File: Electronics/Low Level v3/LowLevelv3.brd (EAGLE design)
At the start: 116.8 x 69.8 mm, 65 parts, among them IC2 MCP4802, K1 ORWH-SH-105D1F,000, K3 ORWH-SH-105D1F,000, Q1 16MHz, T1 2N3904, T2 2N3904, U1 284512-4, U4 MCP2515, U5 MCP2551DIL08, X3 Motor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

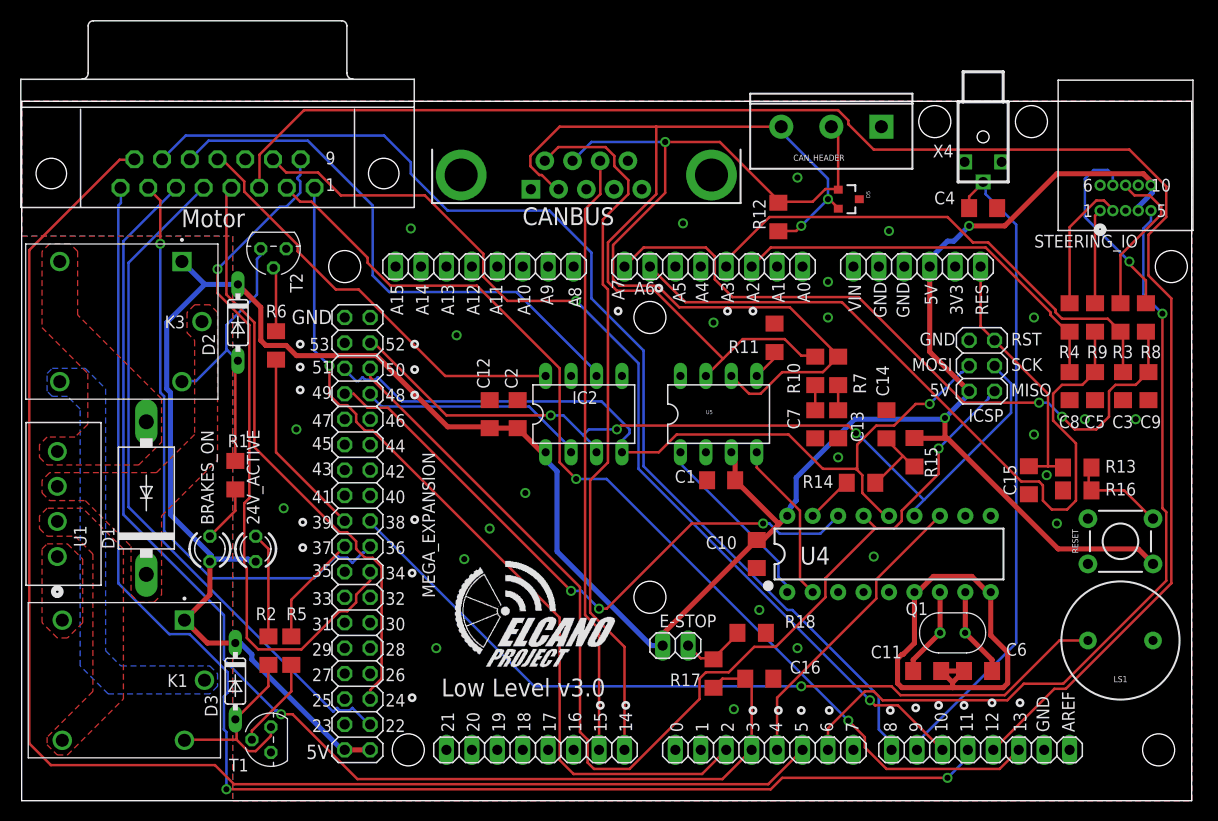
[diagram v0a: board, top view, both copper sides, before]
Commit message: re-routed watchdog from digi-5 to DB15 thru middle instead of along edge
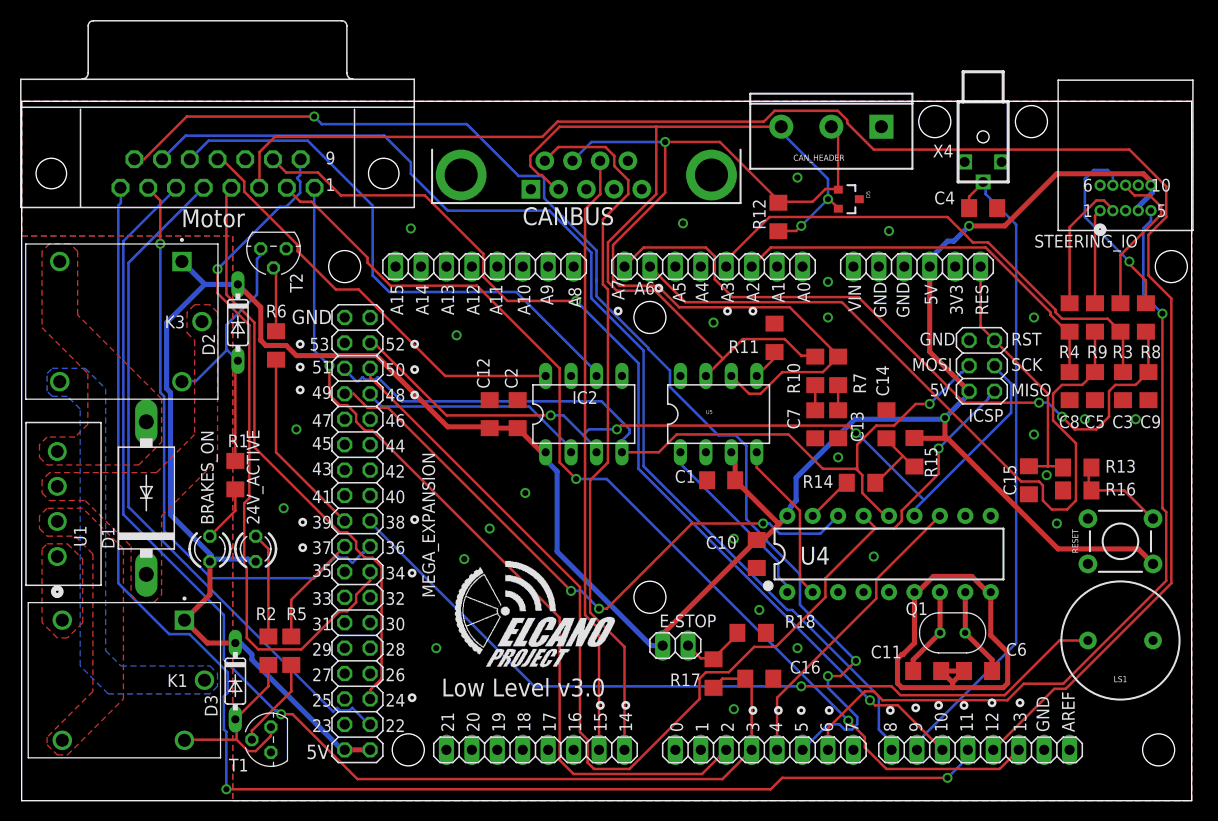
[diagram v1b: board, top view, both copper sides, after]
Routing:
- net WATCHDOG: track 143.8 -> 123.7 mm, vias 0 -> 3
- net GND: vias 25 -> 26
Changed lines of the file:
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@@
 <circle x="73.025" y="9.017" radius="0.315628125" width="0.254" layer="25"/>
 <polygon width="0.254" layer="41">
-<vertex x="3.048" y="3.81"/>
+<vertex x="0" y="3.81"/>
 <vertex x="4.826" y="3.81"/>
 <vertex x="10.922" y="9.906"/>
@@
 <vertex x="14.478" y="41.148"/>
 <vertex x="14.478" y="41.656"/>
-<vertex x="13.716" y="41.656"/>
-<vertex x="6.35" y="49.022"/>
-<vertex x="6.35" y="54.864"/>
-<vertex x="4.826" y="56.388"/>
-<vertex x="2.54" y="56.388"/>
-<vertex x="1.27" y="55.118"/>
-<vertex x="1.27" y="46.736"/>
+<vertex x="7.874" y="48.26"/>
+<vertex x="7.874" y="56.134"/>
+<vertex x="0" y="56.134"/>
+<vertex x="0" y="48.006"/>
 <vertex x="5.842" y="42.164"/>
 <vertex x="5.842" y="37.846"/>
@@
 <vertex x="4.572" y="15.494"/>
 <vertex x="6.35" y="13.716"/>
-<vertex x="6.35" y="11.43"/>
-<vertex x="1.778" y="6.858"/>
-<vertex x="1.778" y="5.08"/>
+<vertex x="6.35" y="12.7"/>
+<vertex x="0" y="6.35"/>
 </polygon>
 <polygon width="0.254" layer="42">
-<vertex x="3.048" y="43.434"/>
+<vertex x="2.286" y="43.434"/>
 <vertex x="6.604" y="43.434"/>
 <vertex x="8.636" y="41.402"/>
@@
 <vertex x="8.89" y="14.986"/>
 <vertex x="9.906" y="13.97"/>
-<vertex x="10.16" y="13.97"/>
 <vertex x="18.542" y="13.97"/>
 <vertex x="19.812" y="12.7"/>
 <vertex x="19.812" y="11.176"/>
 <vertex x="19.05" y="10.414"/>
-<vertex x="18.542" y="10.414"/>
 <vertex x="8.636" y="10.414"/>
 <vertex x="5.588" y="13.462"/>
 <vertex x="5.588" y="38.862"/>
-<vertex x="4.572" y="39.878"/>
 <vertex x="4.318" y="40.132"/>
 <vertex x="3.048" y="40.132"/>
-<vertex x="2.286" y="40.894"/>
-<vertex x="2.286" y="42.926"/>
-<vertex x="2.032" y="43.18"/>
-<vertex x="2.032" y="40.386"/>
-<vertex x="2.794" y="39.624"/>
+<vertex x="2.032" y="41.148"/>
+<vertex x="2.032" y="42.672"/>
+<vertex x="0" y="44.704"/>
+<vertex x="0" y="39.624"/>
 <vertex x="4.318" y="39.624"/>
 <vertex x="5.334" y="38.608"/>
 <vertex x="5.334" y="12.954"/>
 <vertex x="8.382" y="9.906"/>
-<vertex x="8.89" y="9.906"/>
 <vertex x="19.304" y="9.906"/>
-<vertex x="19.812" y="10.414"/>
 <vertex x="20.32" y="10.922"/>
-<vertex x="20.32" y="12.446"/>
 <vertex x="20.32" y="12.7"/>
 <vertex x="18.542" y="14.478"/>
-<vertex x="10.414" y="14.478"/>
-<vertex x="9.144" y="15.748"/>
-<vertex x="9.144" y="20.574"/>
-<vertex x="9.144" y="41.402"/>
-<vertex x="6.858" y="43.688"/>
-<vertex x="3.048" y="43.688"/>
+<vertex x="9.144" y="14.478"/>
+<vertex x="9.144" y="43.02125"/>
+<vertex x="7.96925" y="44.196"/>
+<vertex x="2.286" y="44.196"/>
 </polygon>
 <dimension x1="0" y1="0" x2="116.84" y2="0" x3="58.42" y3="-6.858" textsize="1.778" layer="20" unit="inch"/>
@@
 <via x="77.47" y="62.23" extent="1-16" drill="0.6096"/>
 <via x="101.092" y="36.576" extent="1-16" drill="0.6096"/>
+<via x="71.12" y="26.162" extent="1-16" drill="0.6096"/>
 </signal>
 <signal name="RESET">
@@
 <wire x1="110.617" y1="65.024" x2="114.3" y2="61.341" width="0.254" layer="1"/>
 <wire x1="85.09" y1="65.024" x2="110.617" y2="65.024" width="0.254" layer="1"/>
-<wire x1="82.55" y1="67.564" x2="85.09" y2="65.024" width="0.254" layer="1"/>
-<wire x1="82.55" y1="67.945" x2="82.55" y2="67.564" width="0.254" layer="1"/>
-<wire x1="81.534" y1="68.961" x2="82.55" y2="67.945" width="0.254" layer="1"/>
-<wire x1="28.194" y1="68.961" x2="81.534" y2="68.961" width="0.254" layer="1"/>
-<wire x1="23.749" y1="64.516" x2="28.194" y2="68.961" width="0.254" layer="1"/>
-<wire x1="23.749" y1="61.214" x2="23.749" y2="64.516" width="0.254" layer="1"/>
+<wire x1="82.4395" y1="67.6745" x2="85.09" y2="65.024" width="0.254" layer="1"/>
+<wire x1="23.749" y1="64.77" x2="23.749" y2="61.214" width="0.254" layer="1"/>
 <wire x1="23.749" y1="61.214" x2="23.7109" y2="61.2127" width="0.254" layer="1"/>
+<wire x1="82.4395" y1="67.6745" x2="82.4395" y2="67.96756875" width="0.254" layer="1"/>
+<wire x1="82.4395" y1="67.96756875" x2="81.50956875" y2="68.8975" width="0.254" layer="1"/>
+<wire x1="75.19443125" y1="68.8975" x2="74.11493125" y2="67.818" width="0.254" layer="1"/>
+<wire x1="81.50956875" y1="68.8975" x2="75.19443125" y2="68.8975" width="0.254" layer="1"/>
+<wire x1="53.510575" y1="67.818" x2="51.986575" y2="66.294" width="0.254" layer="1"/>
+<wire x1="74.11493125" y1="67.818" x2="53.510575" y2="67.818" width="0.254" layer="1"/>
+<wire x1="51.986575" y1="66.294" x2="25.273" y2="66.294" width="0.254" layer="1"/>
+<wire x1="25.273" y1="66.294" x2="23.749" y2="64.77" width="0.254" layer="1"/>
 </signal>
 <signal name="REVERSE">
@@
 <contactref element="X3" pad="15"/>
 <contactref element="DIGITAL_0-7" pad="6"/>
-<wire x1="74.549" y1="1.651" x2="77.978" y2="5.08" width="0.254" layer="1"/>
-<wire x1="21.209" y1="1.651" x2="74.549" y2="1.651" width="0.254" layer="1"/>
-<wire x1="19.304" y1="3.556" x2="21.209" y2="1.651" width="0.254" layer="1"/>
-<wire x1="2.921" y1="3.556" x2="19.304" y2="3.556" width="0.254" layer="1"/>
-<wire x1="0.762" y1="5.715" x2="2.921" y2="3.556" width="0.254" layer="1"/>
-<wire x1="0.762" y1="54.991" x2="0.762" y2="5.715" width="0.254" layer="1"/>
-<wire x1="9.779" y1="64.008" x2="0.762" y2="54.991" width="0.254" layer="1"/>
-<wire x1="11.176" y1="64.008" x2="9.779" y2="64.008" width="0.254" layer="1"/>
-<wire x1="11.176" y1="64.008" x2="11.2522" y2="64.0563" width="0.254" layer="1"/>
+<wire x1="11.2522" y1="64.0563" x2="12.2157625" y2="64.0563" width="0.254" layer="1"/>
+<wire x1="12.2157625" y1="64.0563" x2="16.4854625" y2="68.326" width="0.254" layer="1"/>
+<wire x1="16.4854625" y1="68.326" x2="29.21" y2="68.326" width="0.254" layer="1"/>
+<via x="29.21" y="68.326" extent="1-16" drill="0.6096"/>
+<wire x1="29.21" y1="68.326" x2="29.972" y2="67.564" width="0.254" layer="16"/>
+<wire x1="29.972" y1="67.564" x2="44.45" y2="67.564" width="0.254" layer="16"/>
+<wire x1="51.9456125" y1="62.3848" x2="52.1688" y2="62.1616125" width="0.254" layer="16"/>
+<wire x1="44.45" y1="67.564" x2="49.6292" y2="62.3848" width="0.254" layer="16"/>
+<wire x1="49.6292" y1="62.3848" x2="51.9456125" y2="62.3848" width="0.254" layer="16"/>
+<wire x1="52.1688" y1="62.1616125" x2="52.1688" y2="60.182625" width="0.254" layer="16"/>
+<wire x1="52.1688" y1="60.182625" x2="57.404" y2="54.947425" width="0.254" layer="16"/>
+<wire x1="57.404" y1="54.947425" x2="57.404" y2="52.07" width="0.254" layer="16"/>
+<wire x1="57.404" y1="52.07" x2="57.404" y2="51.816" width="0.254" layer="16"/>
+<wire x1="57.404" y1="51.816" x2="57.404" y2="50.375425" width="0.254" layer="16"/>
+<wire x1="57.404" y1="50.375425" x2="62.611" y2="45.168425" width="0.254" layer="16"/>
+<wire x1="62.611" y1="45.168425" x2="62.611" y2="45.085" width="0.254" layer="16"/>
+<wire x1="64.7446" y1="42.9514" x2="64.7446" y2="41.3262375" width="0.254" layer="16"/>
+<wire x1="74.422" y1="26.0477625" x2="74.422" y2="25.908" width="0.254" layer="16"/>
+<wire x1="64.7446" y1="41.3262375" x2="69.5710375" y2="36.4998" width="0.254" layer="16"/>
+<wire x1="69.5710375" y1="36.4998" x2="71.2973625" y2="36.4998" width="0.254" layer="16"/>
+<wire x1="71.2973625" y1="36.4998" x2="72.3646" y2="35.4325625" width="0.254" layer="16"/>
+<wire x1="72.3646" y1="35.4325625" x2="72.3646" y2="28.1051625" width="0.254" layer="16"/>
+<wire x1="72.3646" y1="28.1051625" x2="74.422" y2="26.0477625" width="0.254" layer="16"/>
+<wire x1="62.611" y1="45.085" x2="64.7446" y2="42.9514" width="0.254" layer="16"/>
+<wire x1="74.422" y1="25.908" x2="77.724" y2="22.606" width="0.254" layer="16"/>
+<wire x1="77.724" y1="22.606" x2="77.724" y2="19.558" width="0.254" layer="16"/>
+<wire x1="77.724" y1="19.558" x2="83.312" y2="13.97" width="0.254" layer="16"/>
+<via x="83.312" y="13.97" extent="1-16" drill="0.6096"/>
+<wire x1="83.312" y1="13.97" x2="81.788" y2="12.446" width="0.254" layer="1"/>
+<wire x1="81.788" y1="12.446" x2="80.518" y2="12.446" width="0.254" layer="1"/>
+<via x="80.518" y="12.446" extent="1-16" drill="0.6096"/>
+<wire x1="80.518" y1="7.62" x2="77.978" y2="5.08" width="0.254" layer="16"/>
+<wire x1="83.439" y1="8.3692375" x2="83.439" y2="7.6327625" width="0.254" layer="16"/>
+<wire x1="83.439" y1="7.6327625" x2="82.9182375" y2="7.112" width="0.254" layer="16"/>
+<wire x1="82.9182375" y1="7.112" x2="82.1817625" y2="7.112" width="0.254" layer="16"/>
+<wire x1="80.518" y1="12.446" x2="80.518" y2="11.2902375" width="0.254" layer="16"/>
+<wire x1="82.1817625" y1="7.112" x2="81.6737625" y2="7.62" width="0.254" layer="16"/>
+<wire x1="81.6737625" y1="7.62" x2="80.518" y2="7.62" width="0.254" layer="16"/>
+<wire x1="80.518" y1="11.2902375" x2="83.439" y2="8.3692375" width="0.254" layer="16"/>
 </signal>
 <signal name="WHEELROTATION">

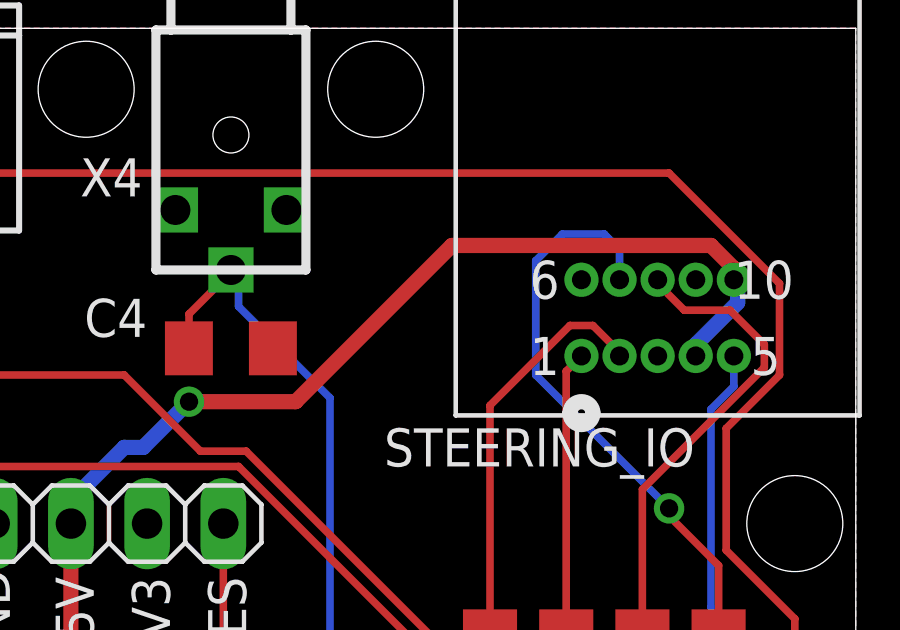
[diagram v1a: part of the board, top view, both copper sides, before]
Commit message: Updates to board, schematic, library
added 4.7k pullup to odometer and took first steps towards replacing the arduino headers with custom component with correct pin names.
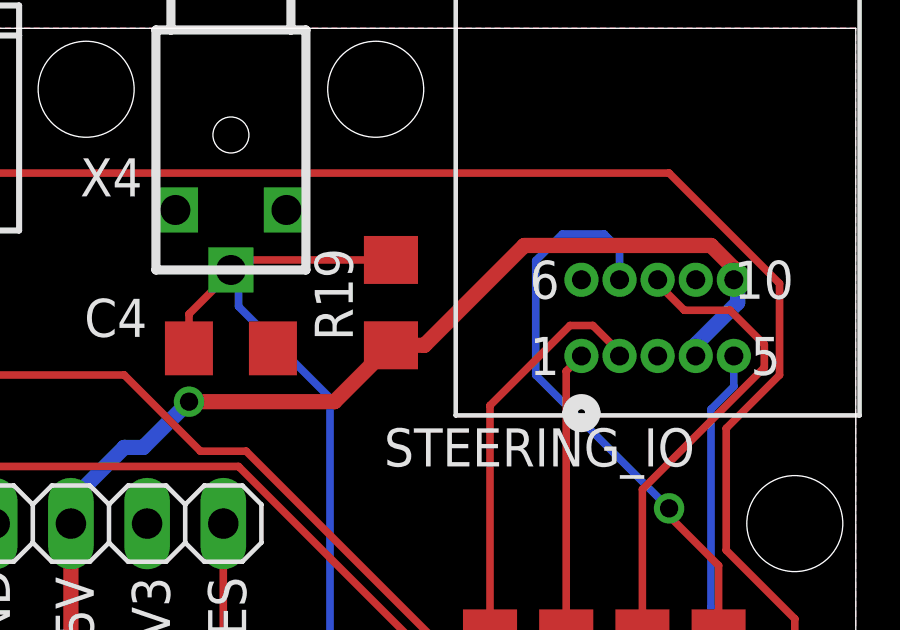
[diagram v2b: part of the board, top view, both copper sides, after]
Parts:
- added R19: 4.7K, resistor:R1206
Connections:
- net 5V: now also R19.1
- net WHEELROTATION: now also R19.2
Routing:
- net WHEELROTATION: track 65.4 -> 70.9 mm
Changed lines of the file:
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@@
 <attribute name="VALUE" x="76.454" y="10.922" size="1.27" layer="27"/>
+</element>
+<element name="R19" library="resistor" library_urn="urn:adsk.eagle:library:348" package="R1206" package3d_urn="urn:adsk.eagle:package:23540/2" value="4.7K" x="101.346" y="60.706" smashed="yes" rot="R90">
+<attribute name="NAME" x="100.076" y="59.436" size="1.27" layer="25" rot="R90"/>
+<attribute name="VALUE" x="103.886" y="59.436" size="1.27" layer="27" rot="R90"/>
 </element>
 </elements>
 <signals>
 <signal name="GND" class="1">
-<contactref element="C4" pad="2"/>
-<contactref element="X4" pad="P$2"/>
-<contactref element="X4" pad="P$3"/>
 <contactref element="U4" pad="9"/>
 <contactref element="CANBUS" pad="3"/>
@@
 <via x="101.092" y="36.576" extent="1-16" drill="0.6096"/>
 <via x="71.12" y="26.162" extent="1-16" drill="0.6096"/>
+<contactref element="C4" pad="2"/>
+<contactref element="X4" pad="P$2"/>
+<contactref element="X4" pad="P$3"/>
 </signal>
 <signal name="RESET">
@@
 <wire x1="96.012" y1="61.722" x2="96.266" y2="61.468" width="0.254" layer="16"/>
 <wire x1="96.012" y1="61.722" x2="96.012" y2="61.794" width="0.254" layer="16"/>
+<contactref element="R19" pad="2"/>
+<wire x1="96.012" y1="61.794" x2="96.346" y2="62.128" width="0.254" layer="1"/>
+<wire x1="96.346" y1="62.128" x2="101.346" y2="62.128" width="0.254" layer="1"/>
 </signal>
 <signal name="R_STR">
@@
 <wire x1="112.776" y1="61.849" x2="112.776" y2="61.468" width="0.508" layer="1"/>
 <wire x1="112.014" y1="62.611" x2="112.776" y2="61.849" width="0.508" layer="1"/>
-<wire x1="103.378" y1="62.611" x2="112.014" y2="62.611" width="0.508" layer="1"/>
-<wire x1="98.171" y1="57.404" x2="103.378" y2="62.611" width="0.508" layer="1"/>
-<wire x1="94.615" y1="57.404" x2="98.171" y2="57.404" width="0.508" layer="1"/>
+<wire x1="105.791" y1="62.611" x2="112.014" y2="62.611" width="0.508" layer="1"/>
 <wire x1="93.091" y1="55.88" x2="94.615" y2="57.404" width="0.508" layer="16"/>
 <wire x1="92.456" y1="55.88" x2="93.091" y2="55.88" width="0.508" layer="16"/>
@@
 <via x="94.615" y="57.404" extent="1-16" drill="0.6096"/>
 <via x="92.202" y="38.227" extent="1-16" drill="0.6096"/>
+<contactref element="R19" pad="1"/>
+<wire x1="99.466" y1="57.404" x2="101.346" y2="59.284" width="0.508" layer="1"/>
+<wire x1="94.615" y1="57.404" x2="99.466" y2="57.404" width="0.508" layer="1"/>
+<wire x1="101.346" y1="59.284" x2="102.464" y2="59.284" width="0.508" layer="1"/>
+<wire x1="102.464" y1="59.284" x2="105.791" y2="62.611" width="0.508" layer="1"/>
 </signal>
 <signal name="HALLPHASEA">
